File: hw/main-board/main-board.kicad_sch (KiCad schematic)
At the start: 66 parts, among them J1 USB_C_Receptacle_USB2.0_16P, J2 S4B-XH-A_LF__SN_, J3 S4B-XH-A_LF__SN_, J4 Conn_ARM_JTAG_SWD_10, Q1 AONR21307, U1 HUSB238_xxxDD, U2 AP63205WU, U3 AP2112K-3.3, U4 PTR54L, U5 TMC2226-SA, U6 TMC2226-SA

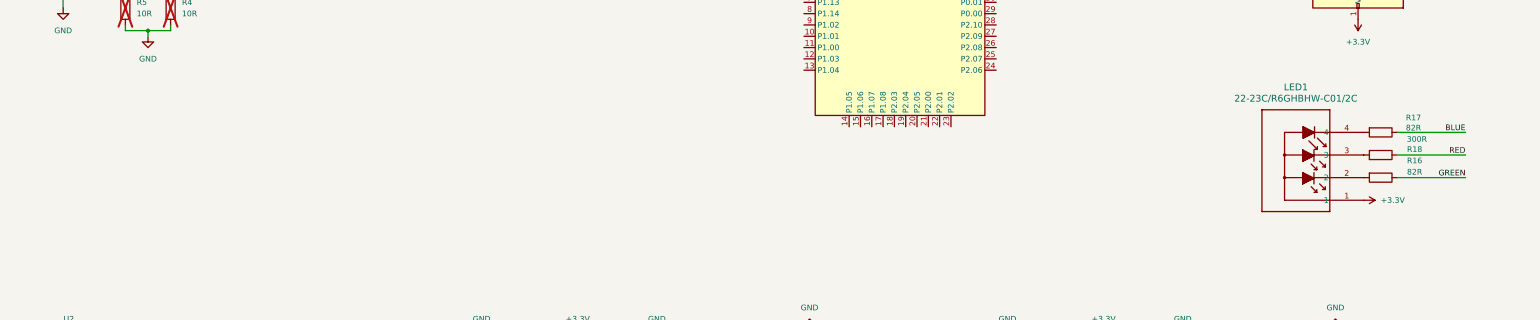
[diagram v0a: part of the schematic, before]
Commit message: Add LED control IC (KTD2026)
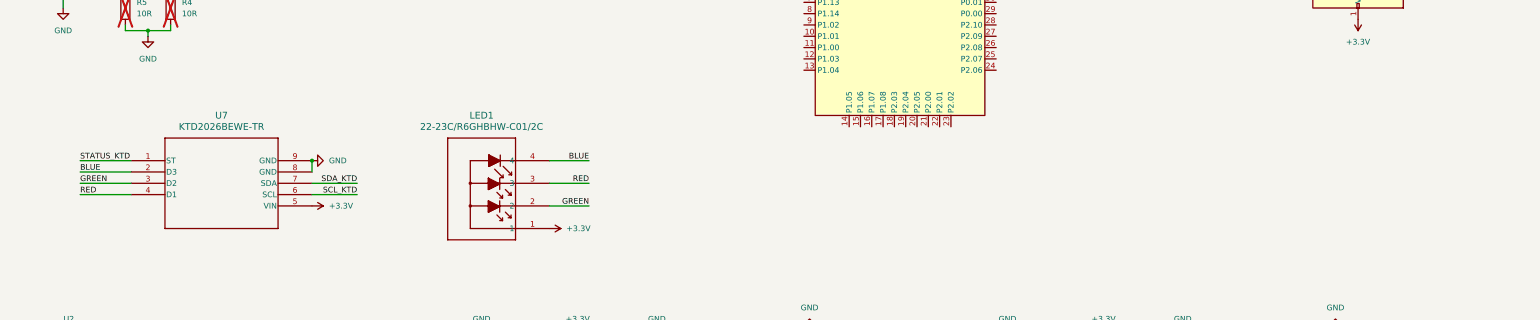
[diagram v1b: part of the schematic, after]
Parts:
- removed R16, R17: 82R, Resistor_SMD:R_0603_1608Metric_Pad0.98x0.95mm_HandSolder, symbol Device:R
- removed R18: 300R, Resistor_SMD:R_0603_1608Metric_Pad0.98x0.95mm_HandSolder, symbol Device:R
- added U7: KTD2026BEWE-TR, Project_Specific_Parts:UTDFN8_1P5X1P5_KIN, symbol Project_Specific_Parts:KTD2026BEWE-TR
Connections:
- net +3.3V: now also U7.5 (VIN)
- net BLUE: now also LED1.4, U7.2 (D3)
- net GND: now also U7.8 (GND), U7.9 (GND)
- net GREEN: now also LED1.2, U7.3 (D2)
- net RED: now also LED1.3, U7.4 (D1)
- new net SCL_KTD: U7.6 (SCL)
- new net SDA_KTD: U7.7 (SDA)
- new net STATUS_KTD: U7.1 (ST)
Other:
- moved on the sheet: LED1

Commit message: Add filtering cap for led ic
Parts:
- added C36: 4.7uF, Capacitor_SMD:C_0805_2012Metric_Pad1.18x1.45mm_HandSolder, symbol Device:C
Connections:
- net +3.3V: now also C36.1
- net GND: now also C36.2
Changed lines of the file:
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@@
 	)
 	(junction
+		(at 133.35 119.38)
+		(diameter 0)
+		(color 0 0 0 0)
+	)
+	(junction
 		(at 135.89 44.45)
 		(diameter 0)
@@
 	)
 	(symbol
+		(lib_id "Device:C")
+		(at 133.35 123.19 0)
+		(unit 1)
+		(body_style 1)
+		(exclude_from_sim no)
+		(in_bom yes)
+		(on_board yes)
+		(in_pos_files yes)
+		(dnp no)
+		(fields_autoplaced yes)
+		(property "Reference" "C36"
+			(at 137.16 121.9199 0)
+			(show_name no)
+			(do_not_autoplace no)
+			(effects
+				(font
+					(size 1.27 1.27)
+				)
+				(justify left)
+			)
+		)
+		(property "Value" "4.7uF"
+			(at 137.16 124.4599 0)
+			(show_name no)
+			(do_not_autoplace no)
+			(effects
+				(font
+					(size 1.27 1.27)
+				)
+				(justify left)
+			)
+		)
+		(property "Footprint" "Capacitor_SMD:C_0805_2012Metric_Pad1.18x1.45mm_HandSolder"
+			(at 134.3152 127 0)
+			(hide yes)
+			(show_name no)
+			(do_not_autoplace no)
+			(effects
+				(font
+					(size 1.27 1.27)
+				)
+			)
+		)
+		(property "Datasheet" ""
+			(at 133.35 123.19 0)
+			(hide yes)
+			(show_name no)
+			(do_not_autoplace no)
+			(effects
+				(font
+					(size 1.27 1.27)
+				)
+			)
+		)
+		(property "Description" "Unpolarized capacitor X7R"
+			(at 133.35 123.19 0)
+			(hide yes)
+			(show_name no)
+			(do_not_autoplace no)
+			(effects
+				(font
+					(size 1.27 1.27)
+				)
+			)
+		)
+		(pin "2"
+		)
+		(pin "1"
+		)
+		(instances
+			(project "main-board"
+				(path "/fe215afa-a228-4dbb-8560-a0753323a3f2"
+					(reference "C36")
+					(unit 1)
+				)
+			)
+		)
+	)
+	(symbol
 		(lib_id "power:+3.3V")
 		(at 368.3 77.47 180)
@@
 					(unit 1)
 				)
+			)
+		)
+	)
+	(symbol
+		(lib_id "power:GND")
+		(at 133.35 127 0)
+		(unit 1)
+		(body_style 1)
+		(exclude_from_sim no)
+		(in_bom yes)
+		(on_board yes)
+		(in_pos_files yes)
+		(dnp no)
+		(fields_autoplaced yes)
+		(property "Reference" "#PWR054"
+			(at 133.35 133.35 0)
+			(hide yes)
+			(show_name no)
+			(do_not_autoplace no)
+			(effects
+				(font
+					(size 1.27 1.27)
+				)
+			)
+		)
+		(property "Value" "GND"
+			(at 133.35 132.08 0)
+			(show_name no)
+			(do_not_autoplace no)
+			(effects
+				(font
+					(size 1.27 1.27)
+				)
+			)
+		)
+		(property "Footprint" ""
+			(at 133.35 127 0)
+			(hide yes)
+			(show_name no)
+			(do_not_autoplace no)
+			(effects
+				(font
+					(size 1.27 1.27)
+				)
+			)
+		)
+		(property "Datasheet" ""
+			(at 133.35 127 0)
+			(hide yes)
+			(show_name no)
+			(do_not_autoplace no)
+			(effects
+				(font
+					(size 1.27 1.27)
+				)
+			)
+		)
+		(property "Description" "Power symbol creates a global label with name \"GND\" , ground"
+			(at 133.35 127 0)
+			(hide yes)
+			(show_name no)
+			(do_not_autoplace no)
+			(effects
+				(font
+					(size 1.27 1.27)
+				)
+			)
+		)
+		(pin "1"
+		)
+		(instances
+			(project "main-board"
+				(path "/fe215afa-a228-4dbb-8560-a0753323a3f2"
+					(reference "#PWR054")
+					(unit 1)
+				)

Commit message: Fix name of nets for TMC2226
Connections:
- net DIAG1: no longer U6.15 (DIAG)
- net DIR1: no longer U6.23 (DIR)
- net EN1: no longer R14.2, U6.5 (~{EN})
- net STEP1: no longer U6.20 (STEP)
- net UART_RX renamed UART_RX1
- net UART_RX1: no longer R11.1, U6.18 (PDN_UART)
- net UART_TX renamed UART_TX1
- net UART_TX1: no longer R11.2
- net VREF renamed VREF1
- net VREF1: no longer C24.2, R15.1, U6.11 (5VOUT)
- new net DIAG2: U6.15 (DIAG)
- new net DIR2: U6.23 (DIR)
- new net EN2: R14.2, U6.5 (~{EN})
- new net STEP2: U6.20 (STEP)
- new net UART_RX2: R11.1, U6.18 (PDN_UART)
- new net UART_TX2: R11.2
- new net VREF2: C24.2, R15.1, U6.11 (5VOUT)
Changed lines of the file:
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@@
 		)
 	)
-	(label "VREF"
+	(label "VREF1"
 		(at 210.82 160.02 0)
 		(effects
@@
 		)
 	)
-	(label "UART_RX"
+	(label "UART_RX1"
 		(at 184.15 185.42 0)
 		(effects
@@
 		)
 	)
-	(label "VREF"
+	(label "VREF2"
 		(at 299.72 218.44 180)
 		(effects
@@
 		)
 	)
-	(label "UART_TX"
+	(label "UART_TX1"
 		(at 171.45 182.88 180)
 		(effects
@@
 		)
 	)
-	(label "DIAG1"
+	(label "DIAG2"
 		(at 307.34 210.82 0)
 		(effects
@@
 		)
 	)
-	(label "DIR1"
+	(label "DIR2"
 		(at 307.34 190.5 0)
 		(effects
@@
 		)
 	)
-	(label "VREF"
+	(label "VREF2"
 		(at 328.93 160.02 0)
 		(effects
@@
 		)
 	)
-	(label "UART_TX"
+	(label "UART_TX2"
 		(at 289.56 182.88 180)
 		(effects
@@
 		)
 	)
-	(label "VREF"
+	(label "VREF1"
 		(at 181.61 218.44 180)
 		(effects
@@
 		)
 	)
-	(label "STEP1"
+	(label "STEP2"
 		(at 307.34 187.96 0)
 		(effects
@@
 		)
 	)
-	(label "UART_RX"
+	(label "UART_RX2"
 		(at 302.26 185.42 0)
 		(effects
@@
 		)
 	)
-	(label "EN1"
+	(label "EN2"
 		(at 307.34 203.2 0)
 		(effects
@@
 		(in_pos_files yes)
 		(dnp no)
-		(fields_autoplaced yes)
 		(property "Reference" "U7"
-			(at 113.03 99.06 0)
-			(show_name no)
-			(do_not_autoplace no)
+			(at 104.394 99.568 0)
+			(show_name no)
+			(do_not_autoplace no)

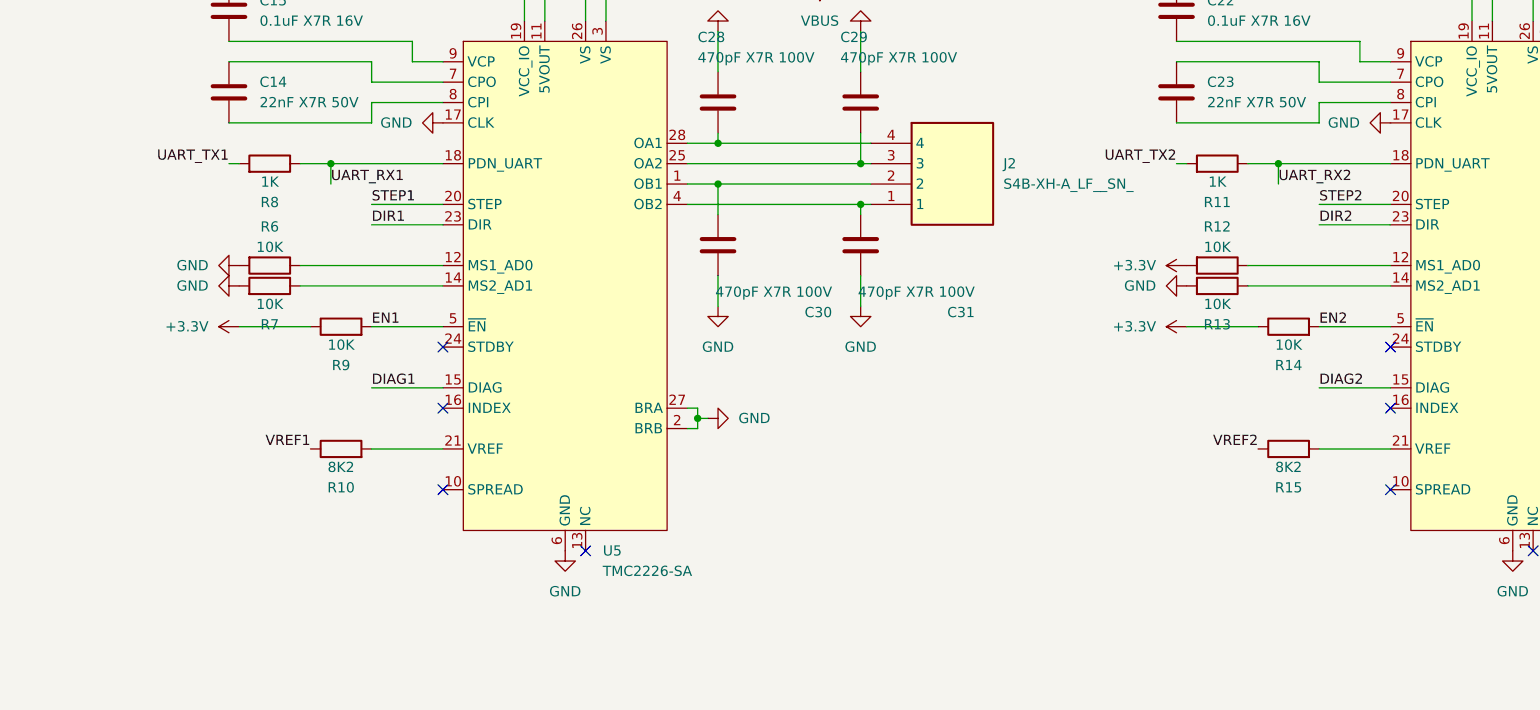
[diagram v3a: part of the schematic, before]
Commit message: Fix UART schematic for TMC2226
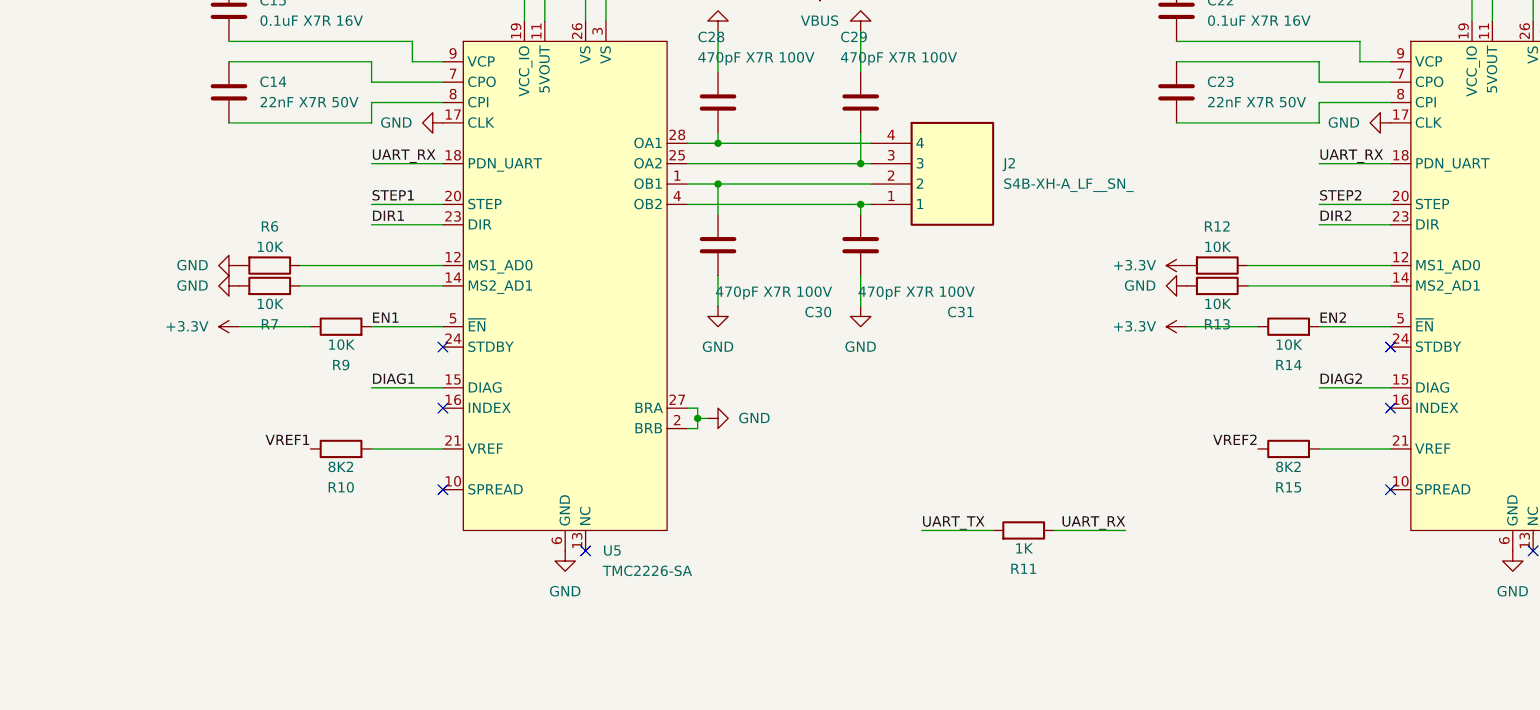
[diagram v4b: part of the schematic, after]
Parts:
- removed R8: 1K, Resistor_SMD:R_0603_1608Metric_Pad0.98x0.95mm_HandSolder, symbol Device:R
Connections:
- net UART_RX2 is gone; now on net UART_RX: R11.1, U6.18 (PDN_UART)
- net UART_RX1 renamed UART_RX
- net UART_TX2 renamed UART_TX
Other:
- moved on the sheet: R11
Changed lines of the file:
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@@
 	)
 	(junction
-		(at 302.26 182.88)
-		(diameter 0)
-		(color 0 0 0 0)
-	)
-	(junction
 		(at 104.14 152.4)
 		(diameter 0)
@@
 	)
 	(junction
-		(at 184.15 182.88)
-		(diameter 0)
-		(color 0 0 0 0)
-	)
-	(junction
 		(at 63.5 232.41)
 		(diameter 0)
@@
 	(wire
 		(pts
-			(xy 298.45 182.88) (xy 302.26 182.88)
-		)
-		(stroke
-			(width 0)
-			(type default)
-		)
-	)
-	(wire
-		(pts
 			(xy 104.14 152.4) (xy 105.41 152.4)
 		)
@@
 	(wire
 		(pts
-			(xy 289.56 182.88) (xy 290.83 182.88)
+			(xy 102.87 52.07) (xy 106.68 52.07)
 		)
 		(stroke
@@
 	(wire
 		(pts
-			(xy 102.87 52.07) (xy 106.68 52.07)
+			(xy 63.5 240.03) (xy 63.5 242.57)
 		)
 		(stroke
@@
 	(wire
 		(pts
-			(xy 63.5 240.03) (xy 63.5 242.57)
+			(xy 232.41 157.48) (xy 232.41 160.02)
 		)
 		(stroke
@@
 	(wire
 		(pts
-			(xy 232.41 157.48) (xy 232.41 160.02)
+			(xy 257.81 228.6) (xy 266.7 228.6)
 		)
 		(stroke
@@
 	(wire
 		(pts
-			(xy 184.15 182.88) (xy 184.15 185.42)
+			(xy 311.15 149.86) (xy 311.15 157.48)
 		)
 		(stroke
@@
 	(wire
 		(pts
-			(xy 311.15 149.86) (xy 311.15 157.48)
+			(xy 274.32 228.6) (xy 283.21 228.6)
 		)
 		(stroke
@@
 	(wire
 		(pts
-			(xy 184.15 182.88) (xy 198.12 182.88)
+			(xy 189.23 182.88) (xy 198.12 182.88)
 		)
 		(stroke
@@
 	(wire
 		(pts
-			(xy 180.34 182.88) (xy 184.15 182.88)
-		)
-		(stroke
-			(width 0)
-			(type default)
-		)
-	)
-	(wire
-		(pts
 			(xy 55.88 57.15) (xy 67.31 57.15)
 		)
@@
 	(wire
 		(pts
-			(xy 302.26 182.88) (xy 316.23 182.88)
+			(xy 307.34 182.88) (xy 316.23 182.88)
 		)
 		(stroke
@@
 	(wire
 		(pts
-			(xy 302.26 182.88) (xy 302.26 185.42)
-		)
-		(stroke
-			(width 0)
-			(type default)
-		)
-	)
-	(wire
-		(pts
 			(xy 233.68 53.34) (xy 233.68 57.15)
 		)
@@
 	(wire
 		(pts
-			(xy 171.45 182.88) (xy 172.72 182.88)
-		)
-		(stroke
-			(width 0)
-			(type default)
-		)
-	)
-	(wire
-		(pts
 			(xy 228.6 185.42) (xy 232.41 185.42)
 		)
@@
 		)
 	)
-	(label "UART_RX1"
-		(at 184.15 185.42 0)
+	(label "UART_RX"
+		(at 189.23 182.88 0)
 		(effects
 			(font
@@
 		)
 	)
-	(label "UART_TX1"
-		(at 171.45 182.88 180)
-		(effects
-			(font
-				(size 1.27 1.27)
-			)
-			(justify right bottom)
-		)
-	)
 	(label "SWDIO"
 		(at 347.98 62.23 0)
@@
 		)
 	)
-	(label "UART_TX2"
-		(at 289.56 182.88 180)
+	(label "UART_RX"
+		(at 283.21 228.6 180)
 		(effects
 			(font
@@
 		)
 	)
+	(label "UART_TX"
+		(at 257.81 228.6 0)
+		(effects
+			(font
+				(size 1.27 1.27)
+			)
+			(justify left bottom)
+		)
+	)
 	(label "GREEN"
 		(at 195.58 119.38 180)
@@
 		)
 	)
-	(label "UART_RX2"
-		(at 302.26 185.42 0)
+	(label "UART_RX"
+		(at 307.34 182.88 0)
 		(effects
 			(font
@@
 	)
 	(symbol
-		(lib_id "Device:R")
-		(at 176.53 182.88 270)
-		(mirror x)
-		(unit 1)
-		(body_style 1)
-		(exclude_from_sim no)
-		(in_bom yes)
-		(on_board yes)
-		(in_pos_files yes)
-		(dnp no)
-		(property "Reference" "R8"
-			(at 176.53 187.706 90)
-			(show_name no)
-			(do_not_autoplace no)
-			(effects
-				(font
-					(size 1.27 1.27)
-				)
-			)
-		)
-		(property "Value" "1K"
-			(at 176.53 185.166 90)
-			(show_name no)
-			(do_not_autoplace no)
-			(effects
-				(font
-					(size 1.27 1.27)
-				)
-			)
-		)
-		(property "Footprint" "Resistor_SMD:R_0603_1608Metric_Pad0.98x0.95mm_HandSolder"
-			(at 176.53 184.658 90)
-			(hide yes)
-			(show_name no)
-			(do_not_autoplace no)
-			(effects
-				(font
-					(size 1.27 1.27)
-				)
-			)
-		)
-		(property "Datasheet" ""
-			(at 176.53 182.88 0)
-			(hide yes)
-			(show_name no)
-			(do_not_autoplace no)
-			(effects
-				(font
-					(size 1.27 1.27)
-				)
-			)
-		)
-		(property "Description" "Resistor"
-			(at 176.53 182.88 0)
-			(hide yes)
-			(show_name no)
-			(do_not_autoplace no)
-			(effects
-				(font
-					(size 1.27 1.27)
-				)
-			)
-		)
-		(pin "1"
-		)
-		(pin "2"
-		)
-		(instances
-			(project "main-board"
-				(path "/fe215afa-a228-4dbb-8560-a0753323a3f2"
-					(reference "R8")
-					(unit 1)
-				)
-			)
-		)
-	)
-	(symbol
 		(lib_id "Regulator_Switching:AP63205WU")
 		(at 78.74 154.94 0)
@@
 	(symbol
 		(lib_id "Device:R")
-		(at 294.64 182.88 270)
+		(at 270.51 228.6 270)
 		(mirror x)
 		(unit 1)
@@
 		(dnp no)
 		(property "Reference" "R11"
-			(at 294.64 187.706 90)
+			(at 270.51 233.426 90)
 			(show_name no)
 			(do_not_autoplace no)
@@
 		)
 		(property "Value" "1K"
-			(at 294.64 185.166 90)
+			(at 270.51 230.886 90)
 			(show_name no)
 			(do_not_autoplace no)
@@
 		)
 		(property "Footprint" "Resistor_SMD:R_0603_1608Metric_Pad0.98x0.95mm_HandSolder"
-			(at 294.64 184.658 90)
+			(at 270.51 230.378 90)
 			(hide yes)
 			(show_name no)
@@
 		)
 		(property "Datasheet" ""
-			(at 294.64 182.88 0)
+			(at 270.51 228.6 0)
 			(hide yes)
 			(show_name no)
@@
 		)
 		(property "Description" "Resistor"
-			(at 294.64 182.88 0)
+			(at 270.51 228.6 0)
 			(hide yes)
 			(show_name no)

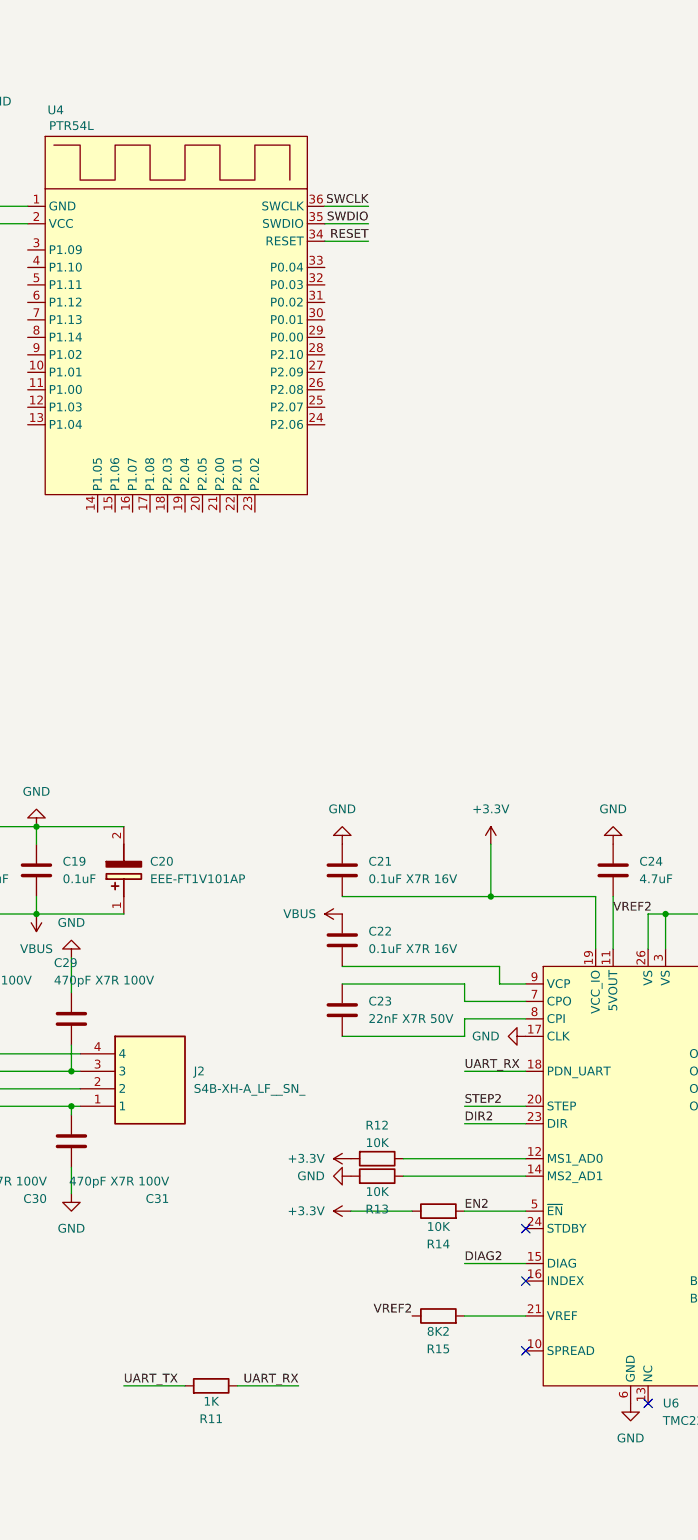
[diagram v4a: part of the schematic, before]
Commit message: Add i2c, uart connections to NRF
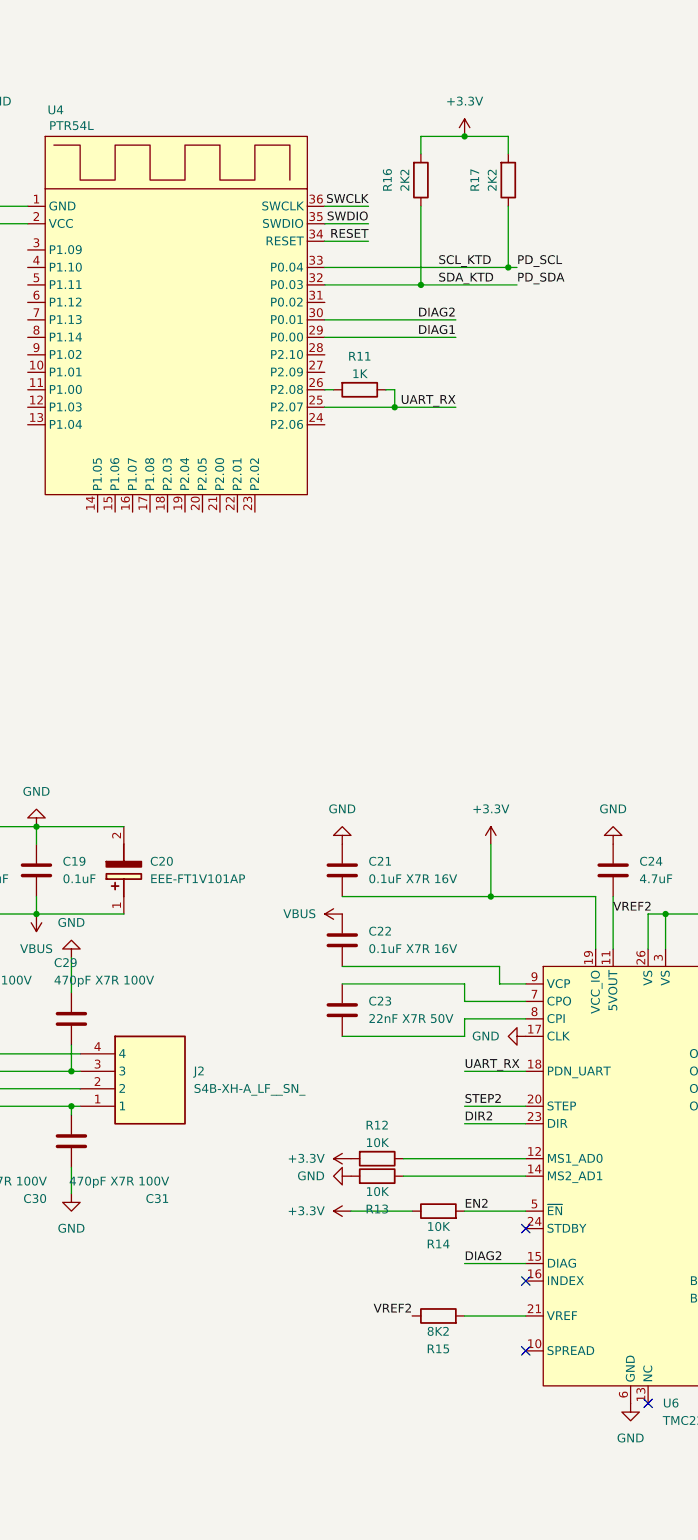
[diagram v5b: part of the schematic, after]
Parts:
- added R16, R17: 2K2, Resistor_SMD:R_0603_1608Metric_Pad0.98x0.95mm_HandSolder, symbol Device:R
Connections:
- net SCL_KTD is gone; now on net PD_SCL: U7.6 (SCL)
- net SDA_KTD is gone; now on net PD_SDA: U7.7 (SDA)
- net UART_TX is gone; now on an unnamed net: R11.2
- net +3.3V: now also R16.2, R17.2
- net DIAG1: now also U4.29 (P0.00)
- net DIAG2: now also U4.30 (P0.01)
- net PD_SCL: now also U4.33 (P0.04), R17.1
- net PD_SDA: now also U4.32 (P0.03), R16.1
- net UART_RX: now also U4.25 (P2.07)
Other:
- moved on the sheet: R11
